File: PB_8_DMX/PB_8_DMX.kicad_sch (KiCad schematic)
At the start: 27 parts, among them J10 USB, J11 RTC Conn, J12 GPIO Header, J13 OLED Select, J9 Pwr In, SW1 OLED Select, SW2 Enter BTN, SW3 Down BTN, U1 Universe5V, U2 24L256

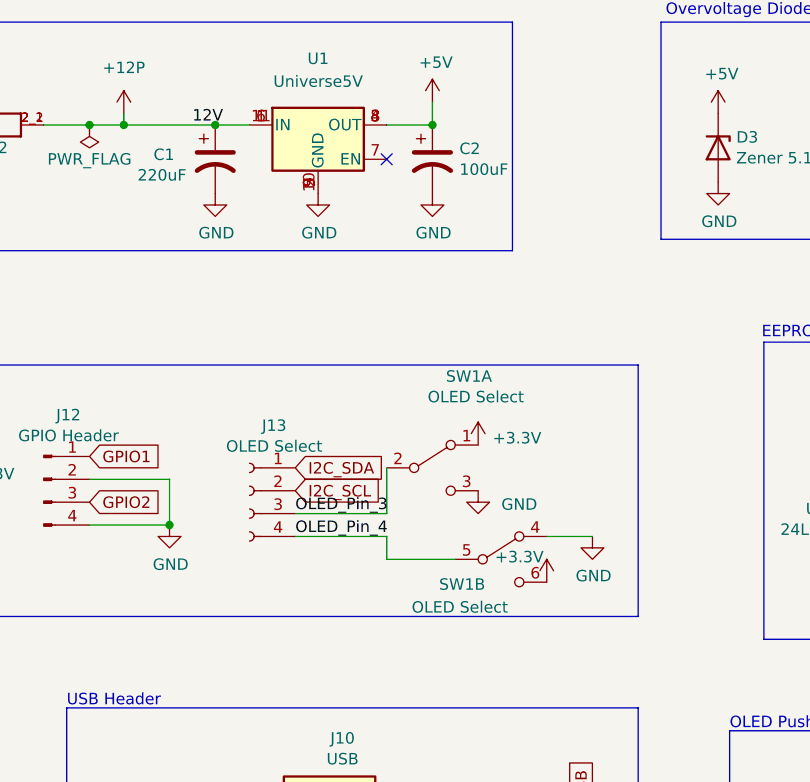
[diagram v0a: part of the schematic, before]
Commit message: remove OLED switch
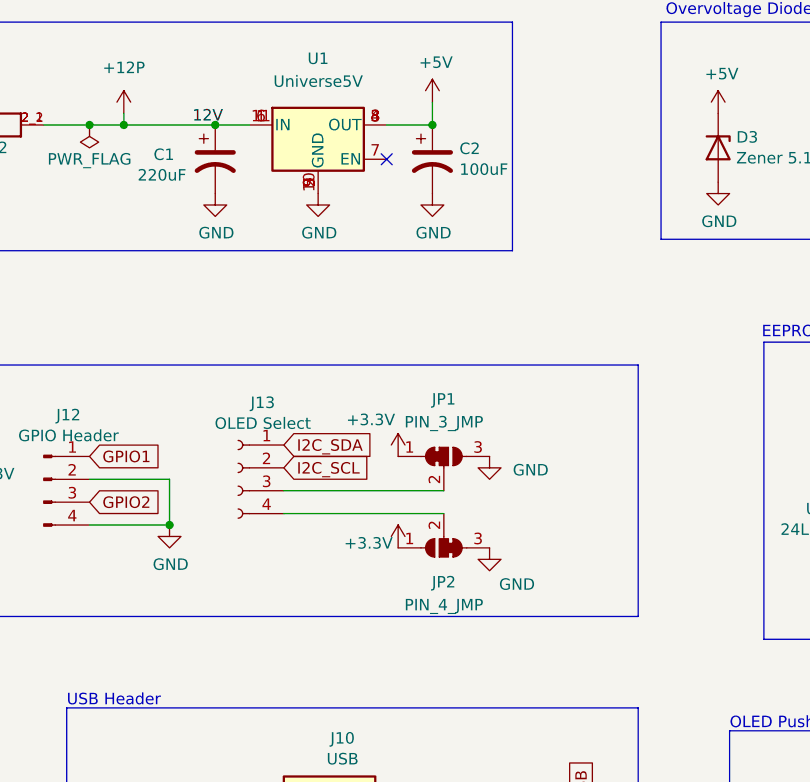
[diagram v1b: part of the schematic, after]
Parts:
- removed SW1: OLED Select, Button_Switch_THT:SW_CuK_JS202011CQN_DPDT_Straight, symbol Switch:SW_DPDT_x2
- added JP1: PIN_3_JMP, Scotts:SolderJumper-3_P1mm_Bridged12, symbol Scotts:SolderJumper_3_Bridged12
- added JP2: PIN_4_JMP, Scotts:SolderJumper-3_P1mm_Bridged23, symbol Scotts:SolderJumper_3_Bridged23
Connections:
- net +3.3V: now also JP1.1 (A), JP2.1 (A)
- net GND: now also JP1.3 (B), JP2.3 (B)
- net OLED_Pin_3: no longer names the net of J13.3 (Pin_3)
- net OLED_Pin_3: now also JP1.2 (C)
- net OLED_Pin_4: no longer names the net of J13.4 (Pin_4)
- net OLED_Pin_4: now also JP2.2 (C)
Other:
- moved on the sheet: J13
